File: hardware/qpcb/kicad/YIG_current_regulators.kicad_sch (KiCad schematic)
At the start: 0 parts

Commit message: Complete PSU simulations and fix ERC errors
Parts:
- added C42, C46: 100p, Capacitor_SMD:C_0805_2012Metric_Pad1.18x1.45mm_HandSolder, symbol Device:C
- added C43: 150n, Capacitor_SMD:C_0805_2012Metric_Pad1.18x1.45mm_HandSolder, symbol Device:C
- added C49: 1u, Capacitor_SMD:C_0805_2012Metric_Pad1.18x1.45mm_HandSolder, symbol Device:C
- added IC9: DAC8562TDGSR, footprints:SOP50P490X110-10N, symbol DAC8562T:DAC8562TDGSR
- added J11, J12: Conn_01x04, symbol Connector_Generic:Conn_01x04
- added Q7, Q8: NPN, Package_TO_SOT_SMD:SOT-23, symbol Simulation_SPICE:NPN
- added R36, R40: 1k, Resistor_SMD:R_0805_2012Metric_Pad1.20x1.40mm_HandSolder, symbol Device:R
- added R37, R41: 33k, Resistor_SMD:R_0805_2012Metric_Pad1.20x1.40mm_HandSolder, symbol Device:R
- added R38, R42: 150, Resistor_SMD:R_0805_2012Metric_Pad1.20x1.40mm_HandSolder, symbol Device:R
- added R39, R43: 1, Resistor_SMD:R_0805_2012Metric_Pad1.20x1.40mm_HandSolder, symbol Device:R
- added U4, U5: LT1632CN8-PBF, footprints:PDIP-8_N_LIT, symbol LT1632CN8_PBF:LT1632CN8-PBF
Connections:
- new net: Q8.2 (B), R42.2
- new net: Q8.3 (E), R43.2, U5.2 (-INA)
- new net: R42.1, U5.1 (OUTA)
- new net: R36.2, R37.1, U4.3 (+INA)
- new net: Q7.3 (E), R39.2, U4.2 (-INA)
- new net: R38.1, U4.1 (OUTA)
- new net: R40.2, R41.1, U5.3 (+INA)
- new net: C43.1, IC9.10 (VREFIN/VREFOUT)
- new net: Q7.2 (B), R38.2
- new net 12V: J11.3 (Pin_3), J12.3 (Pin_3)
- new net 24V: J11.1 (Pin_1), J12.1 (Pin_1)
- new net 5V: C42.1, C46.1, C49.1, IC9.9 (AVDD), U4.8 (V+), U5.8 (V+)
- new net CLR_1_n: IC9.5 (~{CLR})
- new net DIN: IC9.8 (DIN)
- new net GND: C42.2, C43.2, C46.2, C49.2, IC9.3 (GND), J11.2 (Pin_2), J12.2 (Pin_2), R36.1, R39.1, R40.1, R43.1, U4.4 (V-), U5.4 (V-)
- new net LDAC_1_n: IC9.4 (~{LDAC})
- new net SCLK: IC9.7 (SCLK)
- new net SYNC_n: IC9.6 (~{SYNC})
- new net VoutA: IC9.1 (VOUTA), R37.2
- new net VoutB: IC9.2 (VOUTB), R41.2
- new net YIG_TUNE_NEG_1: J12.4 (Pin_4), Q7.1 (C)
- new net YIG_TUNE_NEG_2: J11.4 (Pin_4), Q8.1 (C)
- no-connect marks 0 -> 6
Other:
- note added: "Connectors"
- note added: "DACs"
- note added: "External connections"
- note added: "V/I Converters"

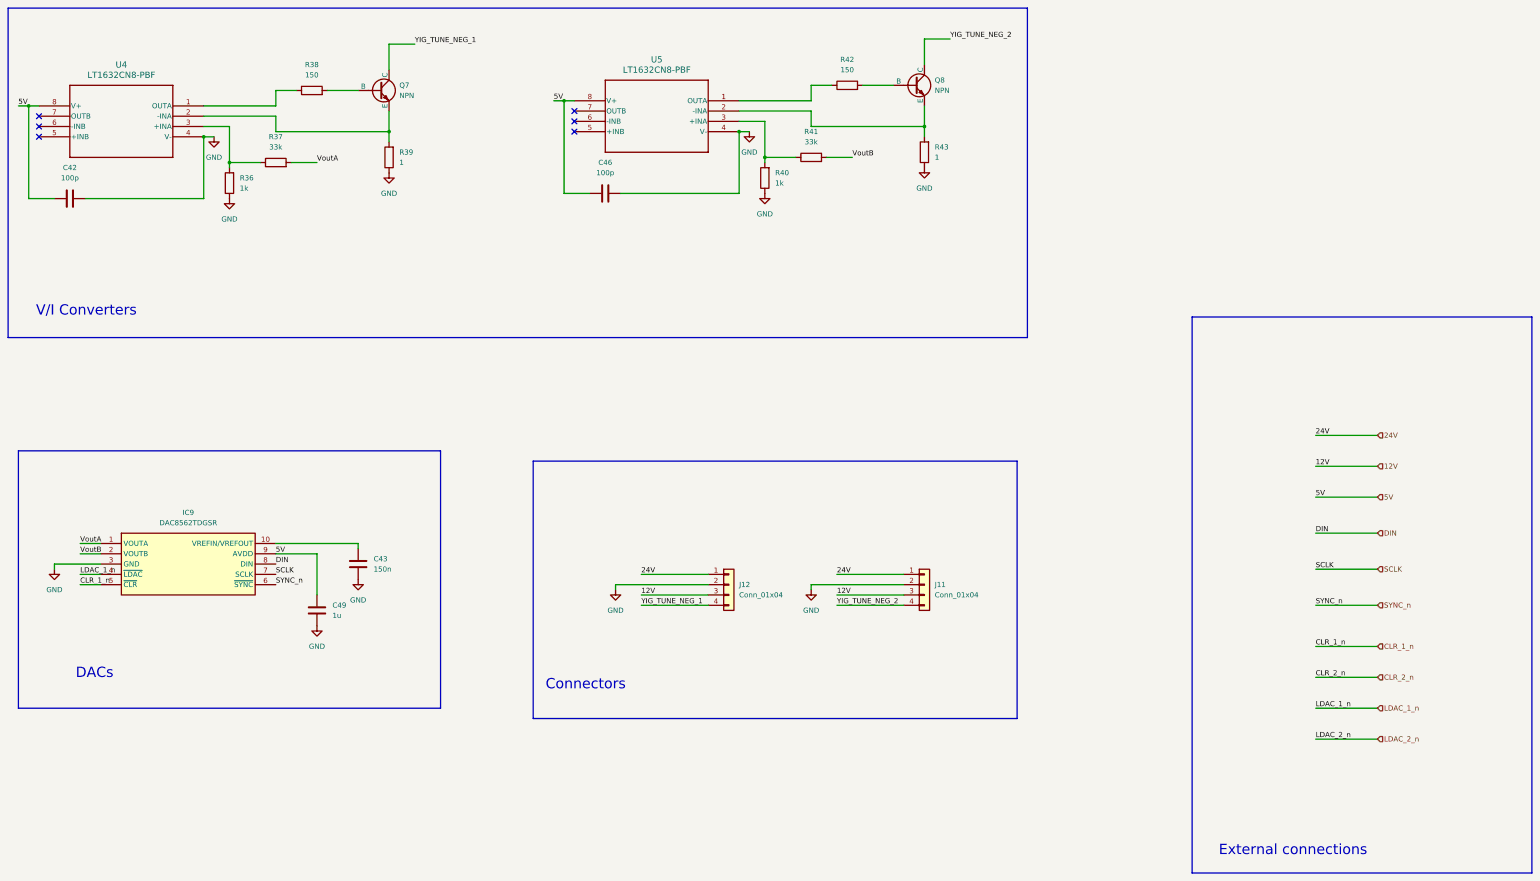
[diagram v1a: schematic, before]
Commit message: Final version of MC43063A and fill components' production info
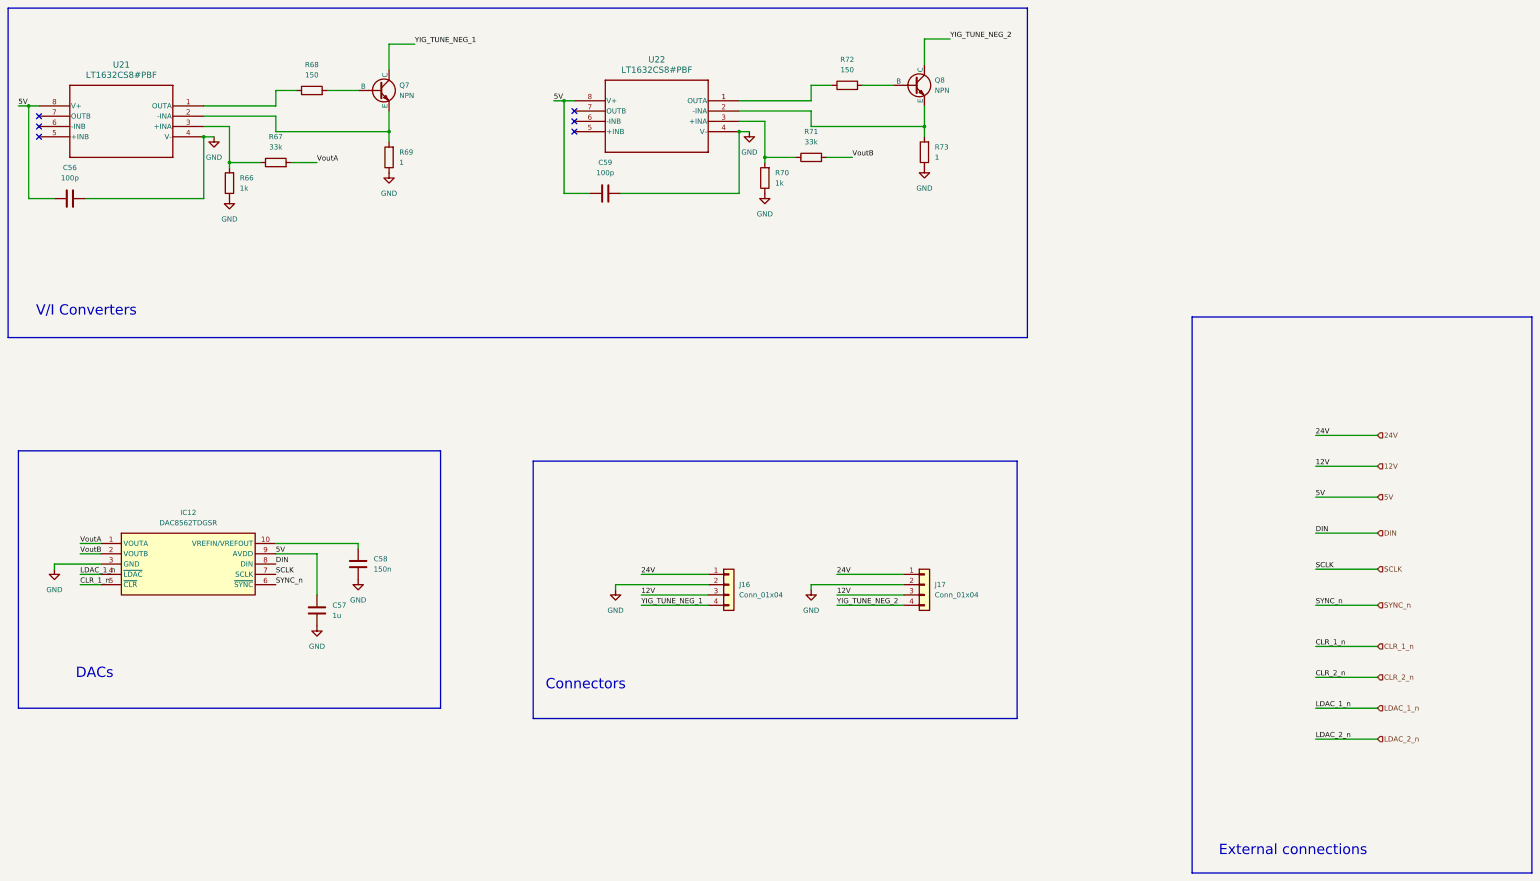
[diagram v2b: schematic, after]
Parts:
- IC12: renamed from IC9; Manufacturer (none) -> Texas Instruments; Manufacturer Part Number (none) -> DAC8562TDGSR; Manufacturer_Name Texas Instruments -> (none); Manufacturer_Part_Number DAC8562TDGSR -> (none); Package (none) -> MSOP-10
- J16: renamed from J12; Manufacturer (none) -> Molex; Manufacturer Part Number (none) -> 47053-1000; Mouser Part Number (none) -> 538-47053-1000; Mouser Price/Stock (none) -> https://www.mouser.it/ProductDetail/Molex/47053-1000?qs=ph4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
- J17: renamed from J11; Manufacturer (none) -> Molex; Manufacturer Part Number (none) -> 47053-1000; Mouser Part Number (none) -> 538-47053-1000; Mouser Price/Stock (none) -> https://www.mouser.it/ProductDetail/Molex/47053-1000?qs=ph4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
- Q7, Q8: Manufacturer (none) -> onsemi; Manufacturer Part Number (none) -> P2N2222A; Mouser Part Number (none) -> P2N2222A; Package (none) -> SOT-23
- U21: renamed from U4; value LT1632CN8-PBF -> LT1632CS8#PBF; Manufacturer (none) -> Analog Devices; Manufacturer Part Number (none) -> LT1632CS8#PBF; Mouser Part Number (none) -> 584-LT1632CS8#PBF; Mouser Price/Stock (none) -> https://www.mouser.it/ProductDetail/Analog-Devices/LT1632CS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; Package (none) -> SOIC-8
- U22: renamed from U5; value LT1632CN8-PBF -> LT1632CS8#PBF; Manufacturer (none) -> Analog Devices; Manufacturer Part Number (none) -> LT1632CS8#PBF; Mouser Part Number (none) -> 584-LT1632CS8#PBF; Mouser Price/Stock (none) -> https://www.mouser.it/ProductDetail/Analog-Devices/LT1632CS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; Package (none) -> SOIC-8
- renumbered C42 to C56, C49 to C57, C43 to C58, C46 to C59, R36 to R66, R37 to R67, R38 to R68, R39 to R69, R40 to R70, R41 to R71, R42 to R72, R43 to R73

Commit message: Add footprints and 3d CAD models of components
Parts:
- C56, C59: Manufacturer (none) -> KYOCERA AVX; Manufacturer Part Number (none) -> 0805YA101FAT2A; Mouser Part Number (none) -> 581-0805YA101FAT2A; Mouser Price/Stock (none) -> https://www.mouser.it/ProductDetail/KYOCERA-AVX/0805YA101FA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; Package (none) -> 0805
- C58: Manufacturer (none) -> KYOCERA AVX; Manufacturer Part Number (none) -> 0805YC154JAT2A; Mouser Part Number (none) -> 581-0805YC154JAT2A; Mouser Price/Stock (none) -> https://www.mouser.it/ProductDetail/KYOCERA-AVX/0805YC154JA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; Package (none) -> 0805
- J16, J17: footprint (none) -> footprints:470531000; Mating Crimp (none) -> 538-08-50-0113-CT; Mating Part (none) -> 538-47054-1000
- Q7, Q8: footprint Package_TO_SOT_SMD:SOT-23 -> Package_TO_SOT_SMD:SOT-23-3
- R66, R67, R68: footprint Resistor_SMD:R_0805_2012Metric_Pad1.20x1.40mm_HandSolder -> Capacitor_SMD:C_0805_2012Metric_Pad1.18x1.45mm_HandSolder
- R69, R73: footprint Resistor_SMD:R_0805_2012Metric_Pad1.20x1.40mm_HandSolder -> Capacitor_SMD:C_0805_2012Metric_Pad1.18x1.45mm_HandSolder; Manufacturer (none) -> Vishay; Manufacturer Part Number (none) -> CRCW08051R00FKEAHP; Mouser Part Number (none) -> 71-CRCW08051R00FKEAH; Mouser Price/Stock (none) -> https://www.mouser.it/ProductDetail/Vishay-Dale/CRCW08051R0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; Package (none) -> 0805
- U21, U22: footprint footprints:PDIP-8_N_LIT -> footprints:SOIC127P600X175-8N
